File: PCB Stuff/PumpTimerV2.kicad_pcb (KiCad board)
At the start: 4 copper layers, 74 x 50 mm, 34 parts, among them J1 282856-2, J2 282856-2, J3 282856-2, J4 Conn_02x20_Odd_Even, J6 B4B-PH-SM4-TBT(LF)(SN), K1 ADW1205HLW, K2 ADW1205HLW, Q1 DMN67D7L, Q2 DMN67D7L, SW1 TL3305AF160QG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

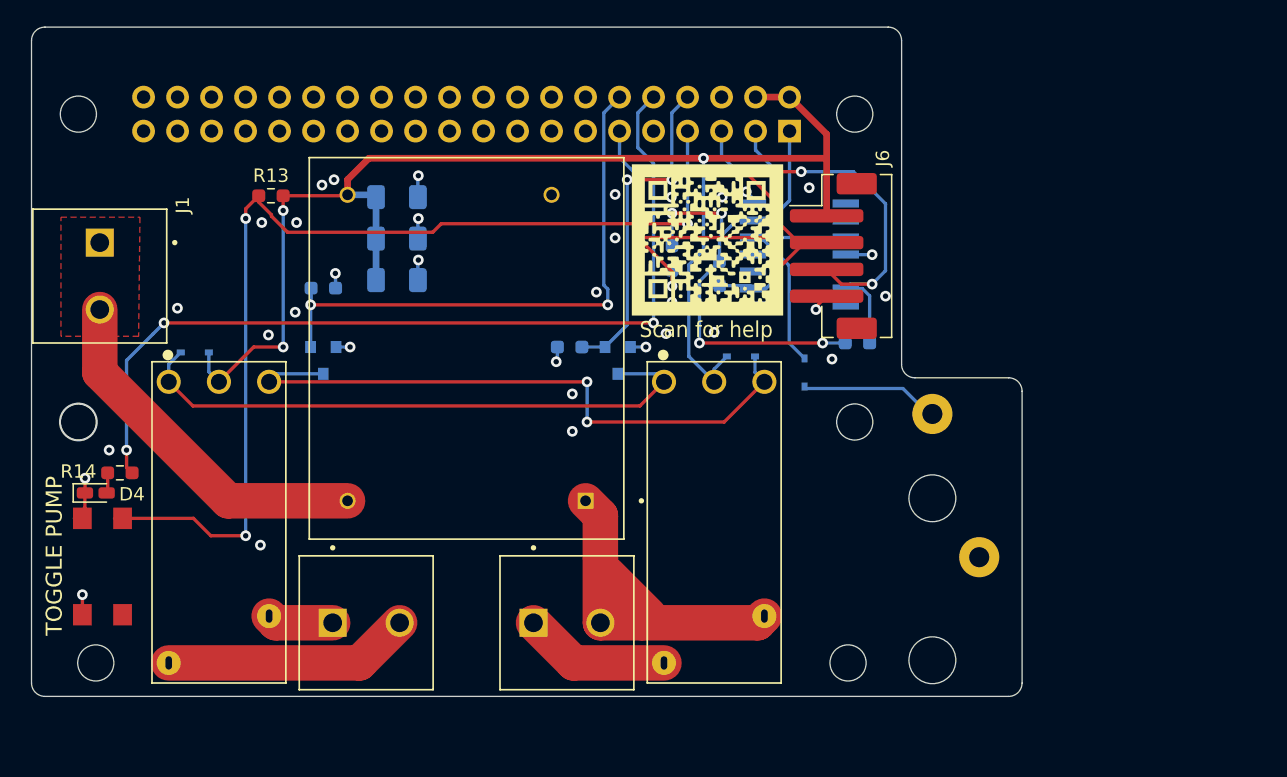
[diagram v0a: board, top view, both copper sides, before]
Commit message: Moving things around to have bigger traces on the AC lines
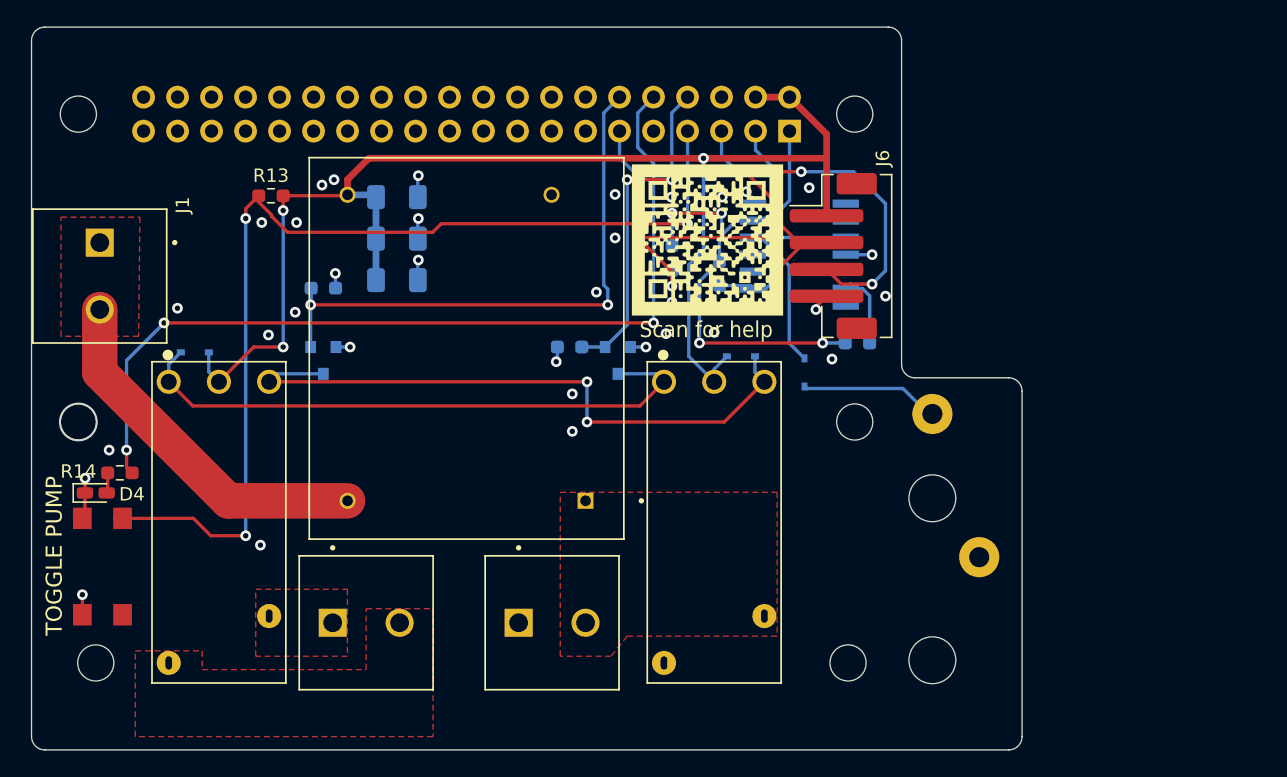
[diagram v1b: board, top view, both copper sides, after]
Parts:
- moved J3 1.11 mm to (78.9, 104.5)
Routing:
- net /Line2_in: track 26.4 -> 0.00 mm
- net /Line1_out: track 18.5 -> 0.00 mm
- net /Line2_out: track 11.0 -> 0.00 mm
- net /Line1_in: track 4.96 -> 0.00 mm
- added copper zone on F.Cu, net /Line1_in
- added copper zone on F.Cu, net /Line1_out
- added copper zone on F.Cu, net /Line2_in
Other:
- board size 74 x 50 mm -> 74 x 54 mm

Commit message: Finished routing bigger AC-line traces
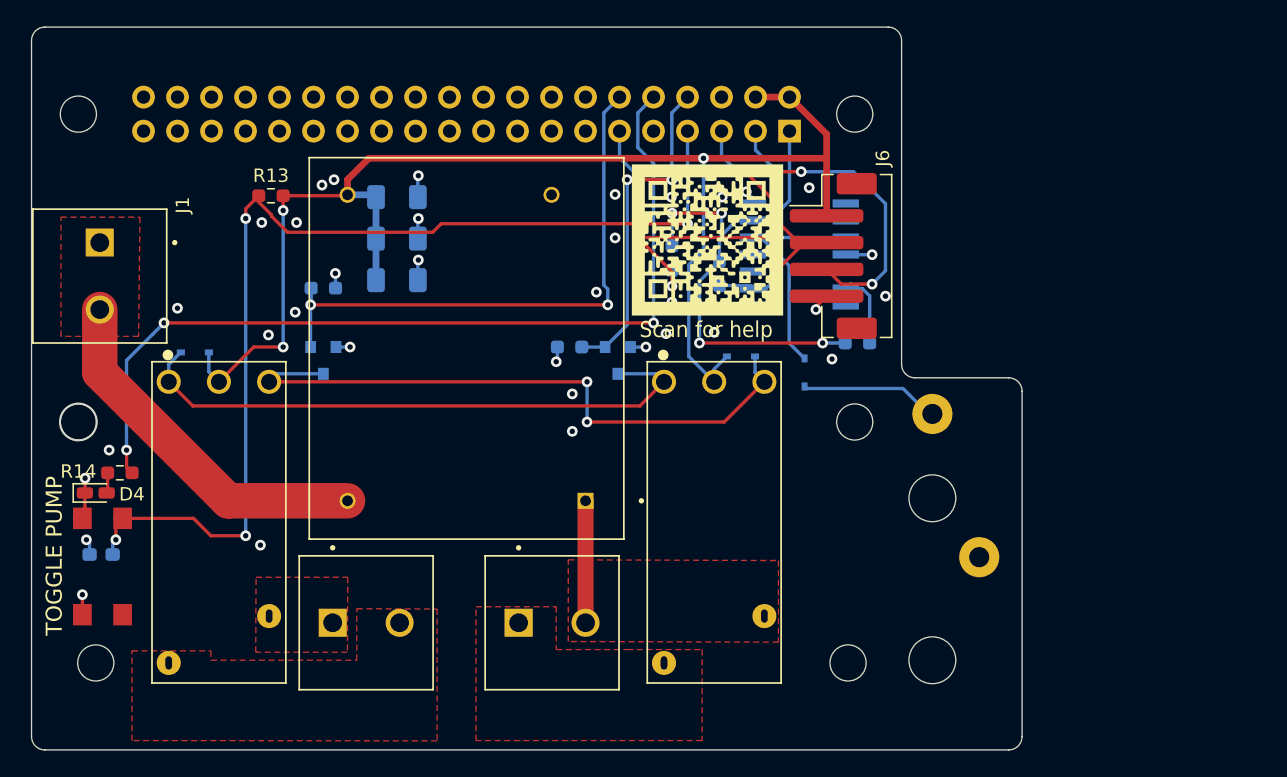
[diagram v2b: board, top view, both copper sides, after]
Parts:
- added C4: 10u, Capacitor_SMD:C_0603_1608Metric_Pad1.08x0.95mm_HandSolder, B.Cu at (45.2, 99.4)
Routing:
- net /Line2_in: track 0.00 -> 9.11 mm
- net /GPIO4: track 77.2 -> 80.2 mm, vias 3 -> 4
- net GND: track 18.7 -> 19.9 mm, vias 37 -> 38
- added copper zone on F.Cu, net /Line2_out

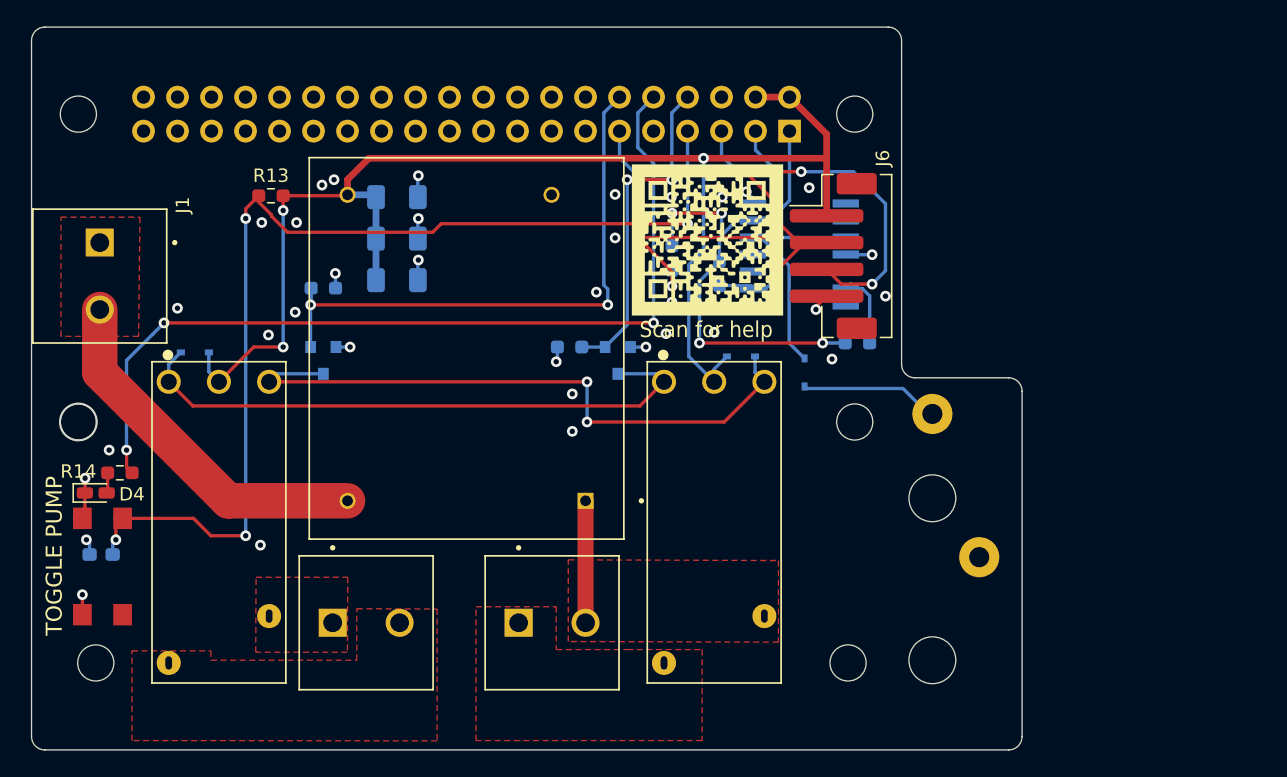
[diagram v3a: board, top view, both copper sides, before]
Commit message: Removed "Neutral" net (my AC/DC converter died. Seems like 230V input is nominal anyways)
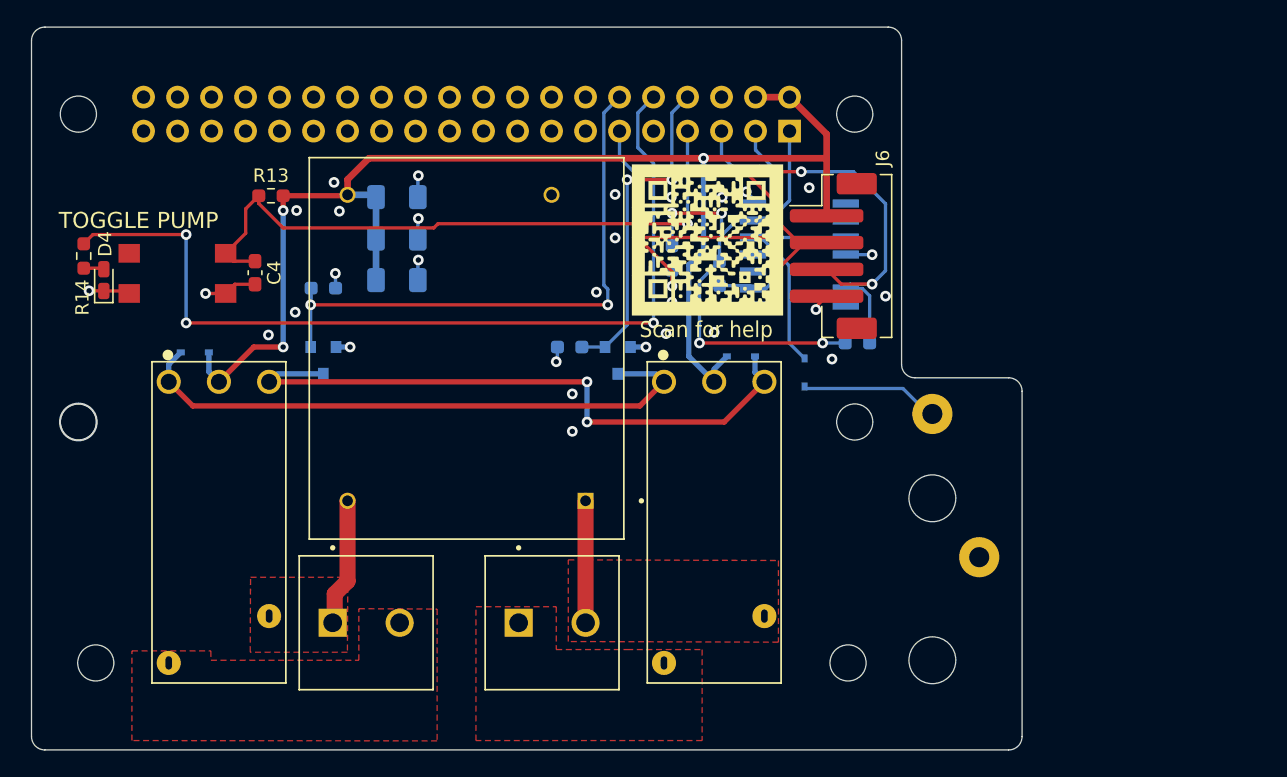
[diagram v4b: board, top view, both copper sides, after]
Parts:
- removed J1: 282856-2, Connector:TE_282856-2
- C4: moved to F.Cu
- moved C4 24.0 mm to (56.7, 78.3), turned to -90 degrees
- moved SW1 22.6 mm to (50.9, 78.4), turned to 0 degrees
- moved R14 16.4 mm to (43.9, 77.1), turned to 90 degrees
- moved D4 15.9 mm to (45.4, 78.9), turned to 90 degrees
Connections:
- net /RTC_~INT~ renamed /RTC_~{INT}
- net /~BTN_RDY~ renamed /~{BTN_RDY}
- PS1 pad 4: /Neutral -> /Line1_in
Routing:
- net /GPIO4: track 80.2 -> 48.2 mm, vias 4 -> 1
- net /Neutral: track 27.2 -> 0.00 mm
- net /Line1_in: track 0.00 -> 9.57 mm
- net GND: track 19.9 -> 20.1 mm, vias 38 -> 33
- removed copper zone on F.Cu, net /Neutral
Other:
- net class Default removed

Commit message: Added temp sensor. Started adding to PCB but not yet placed or routed.
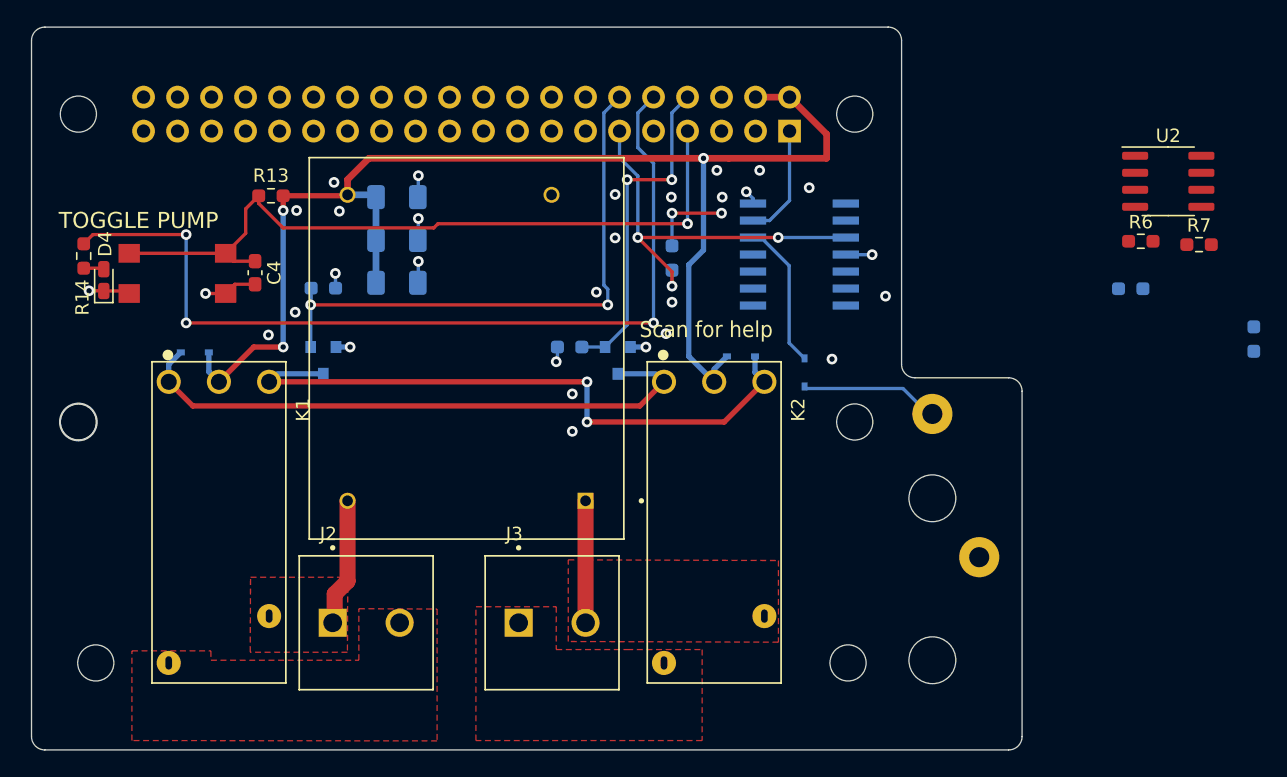
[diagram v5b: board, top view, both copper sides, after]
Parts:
- removed G***: LOGO, Footprints:mediumqr
- removed J6: B4B-PH-SM4-TBT(LF)(SN), Connector_JST:JST_PH_B4B-PH-SM4-TB_1x04-1MP_P2.00mm_Vertical
- added R6: 2k2, Resistor_SMD:R_0603_1608Metric_Pad0.98x0.95mm_HandSolder, F.Cu at (122.9, 76.0)
- added R7: 2k2, Resistor_SMD:R_0603_1608Metric_Pad0.98x0.95mm_HandSolder, F.Cu at (127.2, 76.2)
- added U2: TCN75AVOA, Package_SO:SOIC-8_3.9x4.9mm_P1.27mm, F.Cu at (124.9, 71.5)
- J2, J3: footprint Connector:TE_282856-2 -> Footprints:TE_282856-2
- K1, K2: footprint Relay_THT:RELAY_ADW1205HLW -> Footprints:RELAY_ADW1205HLW
- moved R3 40.2 mm to (131.3, 83.3)
- moved R4 20.8 mm to (122.1, 79.5)
- moved C3 0.20 mm to (67.3, 79.1)
- moved C2 0.10 mm to (67.3, 75.9)
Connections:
- net /RTC_~{INT} renamed /~{RTC_INT}
- J4 pad 13: Net-(J4-Pad13) -> unconnected-(J4-Pad13)
- J4 pad 15: Net-(J4-Pad15) -> unconnected-(J4-Pad15)
- J4 pad 16: Net-(J4-Pad16) -> /~{TEMP_ALERT}
- J4 pad 17: Net-(J4-Pad17) -> unconnected-(J4-Pad17)
- J4 pad 18: Net-(J4-Pad18) -> unconnected-(J4-Pad18)
- J4 pad 19: Net-(J4-Pad19) -> unconnected-(J4-Pad19)
- J4 pad 21: Net-(J4-Pad21) -> unconnected-(J4-Pad21)
- J4 pad 22: Net-(J4-Pad22) -> unconnected-(J4-Pad22)
- J4 pad 23: Net-(J4-Pad23) -> unconnected-(J4-Pad23)
- J4 pad 24: Net-(J4-Pad24) -> unconnected-(J4-Pad24)
- J4 pad 25: Net-(J4-Pad25) -> unconnected-(J4-Pad25)
- J4 pad 26: Net-(J4-Pad26) -> unconnected-(J4-Pad26)
- J4 pad 27: Net-(J4-Pad27) -> unconnected-(J4-Pad27)
- J4 pad 28: Net-(J4-Pad28) -> unconnected-(J4-Pad28)
- J4 pad 29: Net-(J4-Pad29) -> unconnected-(J4-Pad29)
- J4 pad 30: Net-(J4-Pad30) -> unconnected-(J4-Pad30)
- J4 pad 31: Net-(J4-Pad31) -> unconnected-(J4-Pad31)
- J4 pad 32: Net-(J4-Pad32) -> unconnected-(J4-Pad32)
- J4 pad 33: Net-(J4-Pad33) -> unconnected-(J4-Pad33)
- J4 pad 34: Net-(J4-Pad34) -> unconnected-(J4-Pad34)
- J4 pad 35: Net-(J4-Pad35) -> unconnected-(J4-Pad35)
- J4 pad 36: Net-(J4-Pad36) -> unconnected-(J4-Pad36)
- J4 pad 37: Net-(J4-Pad37) -> unconnected-(J4-Pad37)
- J4 pad 38: Net-(J4-Pad38) -> unconnected-(J4-Pad38)
- J4 pad 39: Net-(J4-Pad39) -> unconnected-(J4-Pad39)
- J4 pad 40: Net-(J4-Pad40) -> unconnected-(J4-Pad40)
- U1 pad 3: Net-(U1-Pad3) -> unconnected-(U1-Pad3)
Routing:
- net /GPIO2(SDA1): track 30.7 -> 0.04 mm, vias 3 -> 0
- net +3V3: track 39.0 -> 14.7 mm, vias 4 -> 2
- net /GPIO3(SCL1): track 23.0 -> 0.00 mm, vias 2 -> 0
- net /GPIO4: track 48.2 -> 55.4 mm
- net +5VD: track 103.6 -> 99.4 mm
- net GND: track 20.1 -> 19.1 mm, vias 33 -> 30

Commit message: Rerouted PCB with temp sensor in place
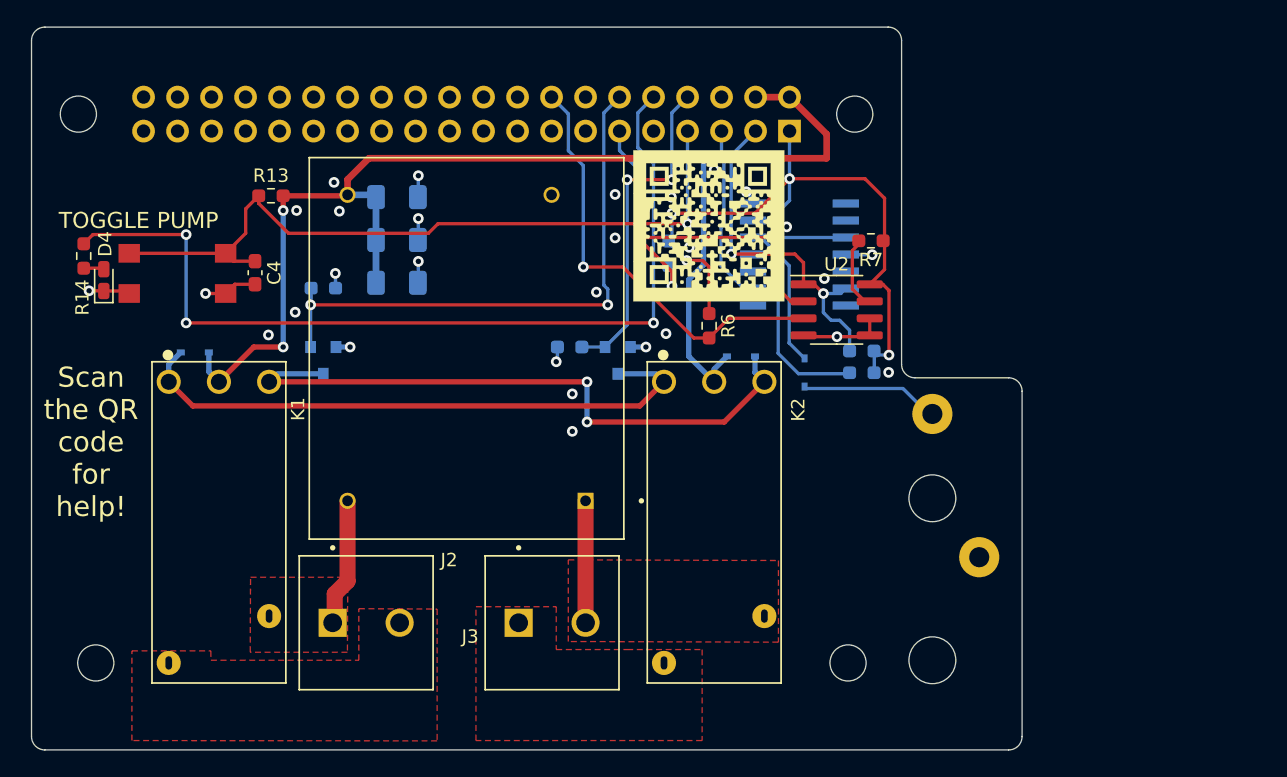
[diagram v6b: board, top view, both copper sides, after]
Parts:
- removed the H2 at (101.5, 89.5)
- removed H5: 2.75mm Mount, MountingHole:MountingHole_2.7mm_M2.5
- added G***: LOGO, Footprints:QR_PumpTimerV2, F.Cu at (90.6, 74.8)
- moved R6 32.9 mm to (90.6, 82.3), turned to -90 degrees
- moved R3 29.4 mm to (102.0, 85.8), turned to 180 degrees
- moved U2 26.6 mm to (100.1, 81.1)
- moved R7 24.5 mm to (102.7, 76.0), turned to 180 degrees
- moved R4 20.6 mm to (102.0, 84.2), turned to 180 degrees
- moved R5 0.43 mm to (87.6, 76.9)
- renumbered H3 to H2, H4 to H3, H6 to H4
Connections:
- U2 pad 8: +3.3V -> +3V3
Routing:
- net +3V3: track 14.7 -> 51.3 mm, vias 2 -> 4
- net /~{TEMP_ALERT}: track 0.00 -> 32.9 mm, vias 0 -> 1
- net /GPIO3(SCL1): track 0.00 -> 28.3 mm, vias 0 -> 1
- net /GPIO2(SDA1): track 0.04 -> 26.3 mm, vias 0 -> 2
- net Net-(R7-Pad2): track 0.00 -> 5.58 mm
- net GND: track 19.1 -> 24.5 mm, vias 30 -> 29
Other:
- outline, holes or cut-outs redrawn
- board text added: "Scan the QR code for help!"
- board text removed: "Scan for help"
